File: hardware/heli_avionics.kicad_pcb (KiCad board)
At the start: 4 copper layers, 65.5 x 39 mm, 70 parts, among them J1 Pin_Header_2x3, J2 JST_PH_01x02, J3 JST_XH_01x02, J4 JST_XH_01x02, J5 JST_PH_01x03, J6 Conn_01x01, J7 JST_ZH_01x02, J8 Conn_01x01, Q1 AO3400A, SW1 Reset, U1 ATmega4808-A, U2 nRF24L01P, U3 DRV8212, U4 DRV8212, U5 BMP390L, U6 TPS7A2030PDBV, U7 TPS7A2030PDBV, Y1 16MHz

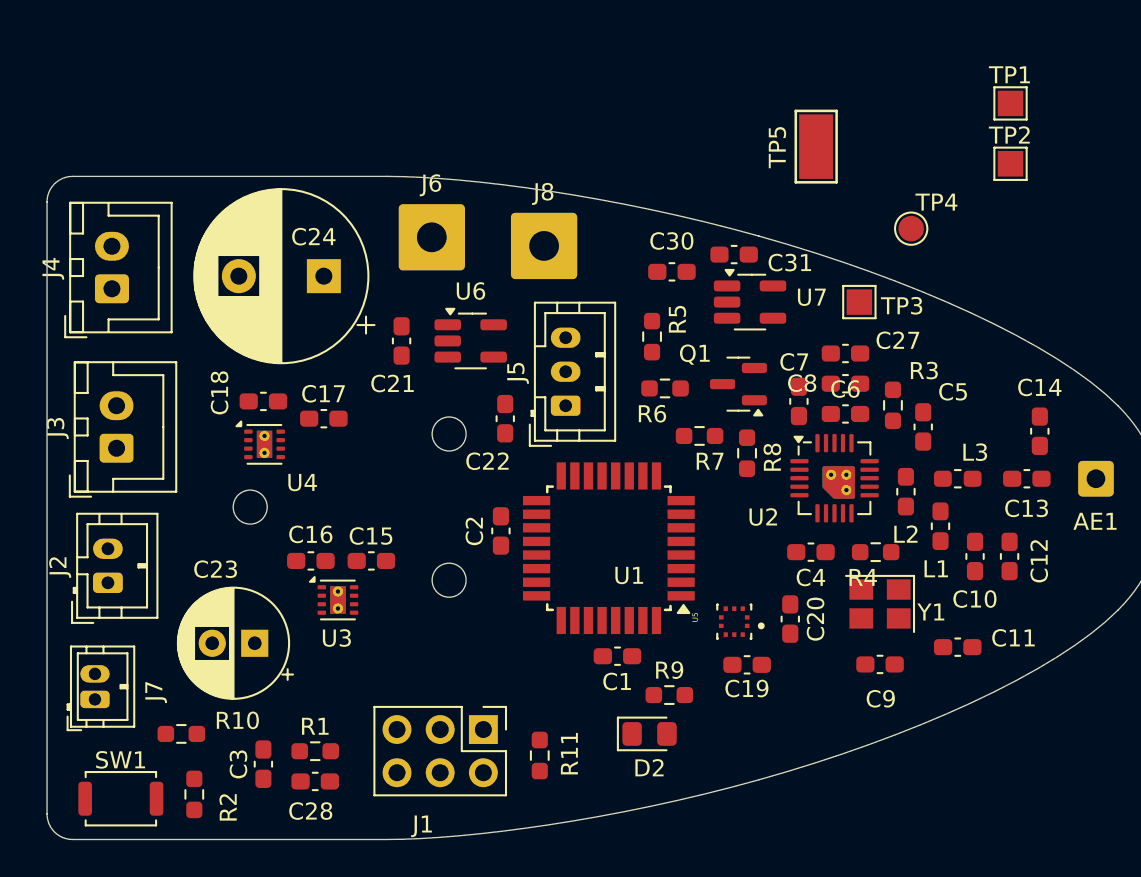
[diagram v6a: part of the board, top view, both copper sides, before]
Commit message: Reordered some MCU pin connections for nicer layout
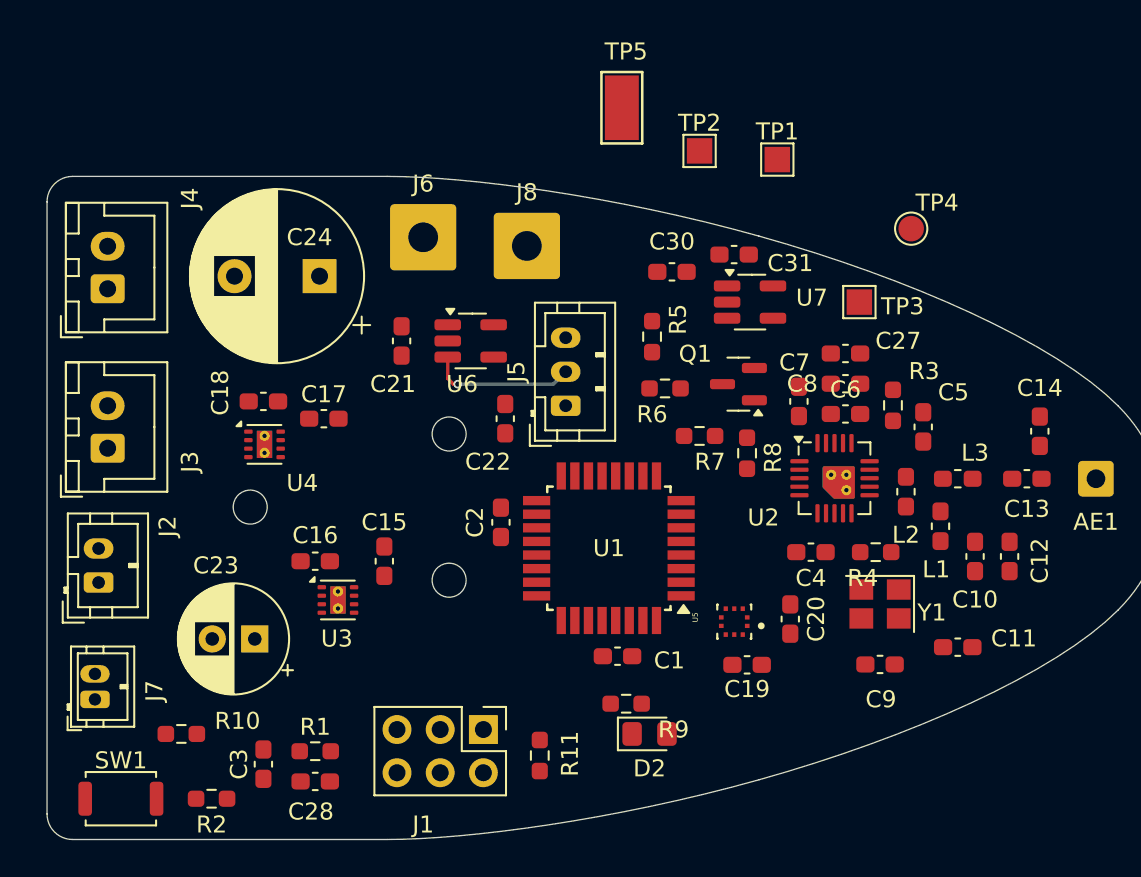
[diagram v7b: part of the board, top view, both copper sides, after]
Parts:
- moved TP2 18.3 mm to (138.4, 98.6)
- moved TP1 14.1 mm to (143.0, 99.1)
- moved TP5 11.7 mm to (133.9, 96.0)
- moved R9 2.59 mm to (134.1, 131.1), turned to 180 degrees
- moved R2 1.05 mm to (109.7, 136.7), turned to 0 degrees
- moved J8 1.02 mm to (128.3, 104.1)
- moved C15 0.76 mm to (119.9, 122.7), turned to 90 degrees
- moved J2 0.55 mm to (103.1, 123.9)
- moved J3 0.53 mm to (103.6, 116.0)
- moved C2 0.51 mm to (126.7, 120.4)
- moved J6 0.51 mm to (122.2, 103.6)
- moved C16 0.25 mm to (115.8, 122.7), turned to 0 degrees
- moved J4 0.25 mm to (103.6, 106.7)
- moved C23 0.25 mm to (112.3, 127.3)
- moved C24 0.25 mm to (116.1, 105.9)
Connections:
- R10 pad 2: /PF4 -> /PF5
- R5 pad 2: /PD7 -> /PD1
- R6 pad 1: /PD7 -> /PD1
- R7 pad 1: /PD6 -> /PD0
- U1 pad 10: unconnected-(U1-PD0-Pad10) -> /PD0
- U1 pad 11: unconnected-(U1-PD1-Pad11) -> /PD1
- U1 pad 23: unconnected-(U1-PF3-Pad23) -> /PF3
- U1 pad 25: unconnected-(U1-PF5-Pad25) -> /PF5
- U3 pad 5: /PD5 -> /PF4
- U3 pad 6: /PD4 -> /PF3
- U4 pad 5: /PD3 -> /PF2
- U4 pad 6: /PD2 -> /PD7
- U4 pad 7: /PF2 -> /PD6
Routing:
- net /Power circuits/VREG_EN: track 0.00 -> 8.63 mm, vias 0 -> 1

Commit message: Pressure sensor now uses i2c
Also rewired nrf24 to use the other SPI
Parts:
- added R12: 4k7, Resistor_SMD:R_0603_1608Metric_Pad0.98x0.95mm_HandSolder, F.Cu at (137.7, 129.3)
- added R13: 4k7, Resistor_SMD:R_0603_1608Metric_Pad0.98x0.95mm_HandSolder, F.Cu at (140.5, 124.7)
- moved C19 3.78 mm to (144.0, 126.2), turned to 0 degrees
- moved C20 3.04 mm to (143.0, 129.0), turned to -90 degrees
- moved D2 1.71 mm to (134.1, 133.9)
- moved R7 1.30 mm to (137.2, 115.1)
- moved U5 1.27 mm to (140.5, 127.5), turned to 0 degrees
- moved R8 1.05 mm to (141.0, 115.3), turned to 180 degrees
- moved C3 0.25 mm to (112.8, 134.9)
- moved C4 0.24 mm to (145.0, 121.9)
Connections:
- R5 pad 2: /PD1 -> /PD2
- R6 pad 1: /PD1 -> /PD2
- R7 pad 1: /PD0 -> /PD1
- U1 pad 1: /PA3 -> /I2C_SCL
- U1 pad 3: /PA5 -> unconnected-(U1-PA5-Pad3)
- U1 pad 32: unconnected-(U1-PA2-Pad32) -> /I2C_SDA
- U1 pad 9: /PC3 -> /SPI_SS
- U2 pad 1: /PA3 -> /PD0
- U2 pad 2: /PA4 -> /SPI_SS
- U2 pad 6: /PA5 -> /PA6
- U5 pad 2: /SPI_CLK -> /I2C_SCL
- U5 pad 4: /SPI_MOSI -> /I2C_SDA
- U5 pad 5: /SPI_MISO -> GND
- U5 pad 6: /PC3 -> VCC
- U5 pad 7: /PA6 -> /PA4
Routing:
- net /PD0: track 0.00 -> 9.08 mm
- net /Power circuits/VREG_EN: track 8.63 -> 13.4 mm
- net /SPI_SS: track 0.00 -> 2.97 mm
